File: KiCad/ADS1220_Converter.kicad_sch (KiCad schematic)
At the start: 10 parts, among them U1 ADS1220xPW

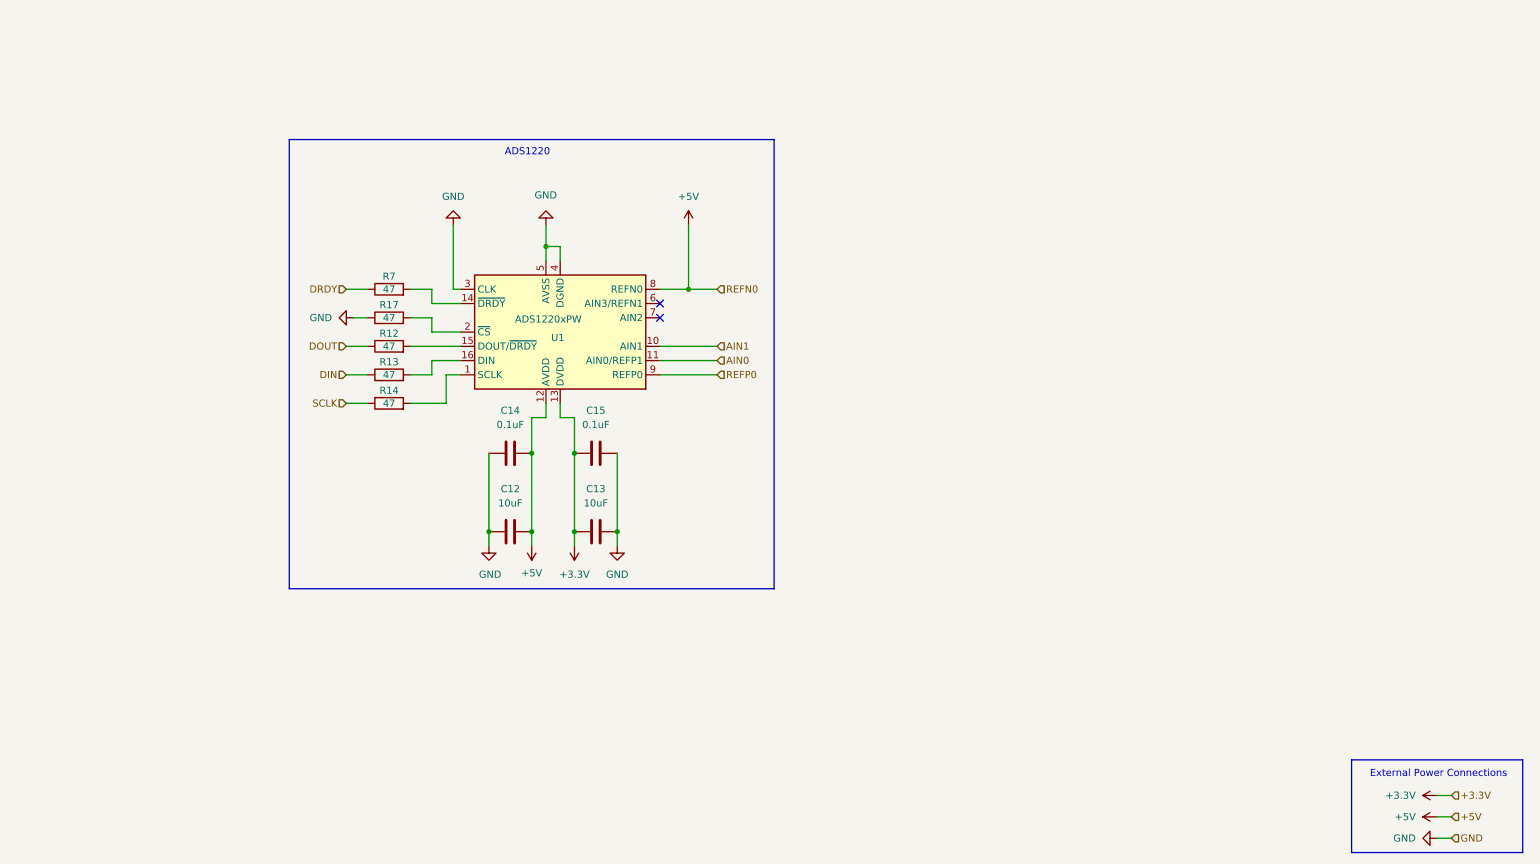
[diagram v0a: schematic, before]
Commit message: Use 12V Power
* Use 12 V Power
* Update to an F103 processor with better compatibility with Katapult
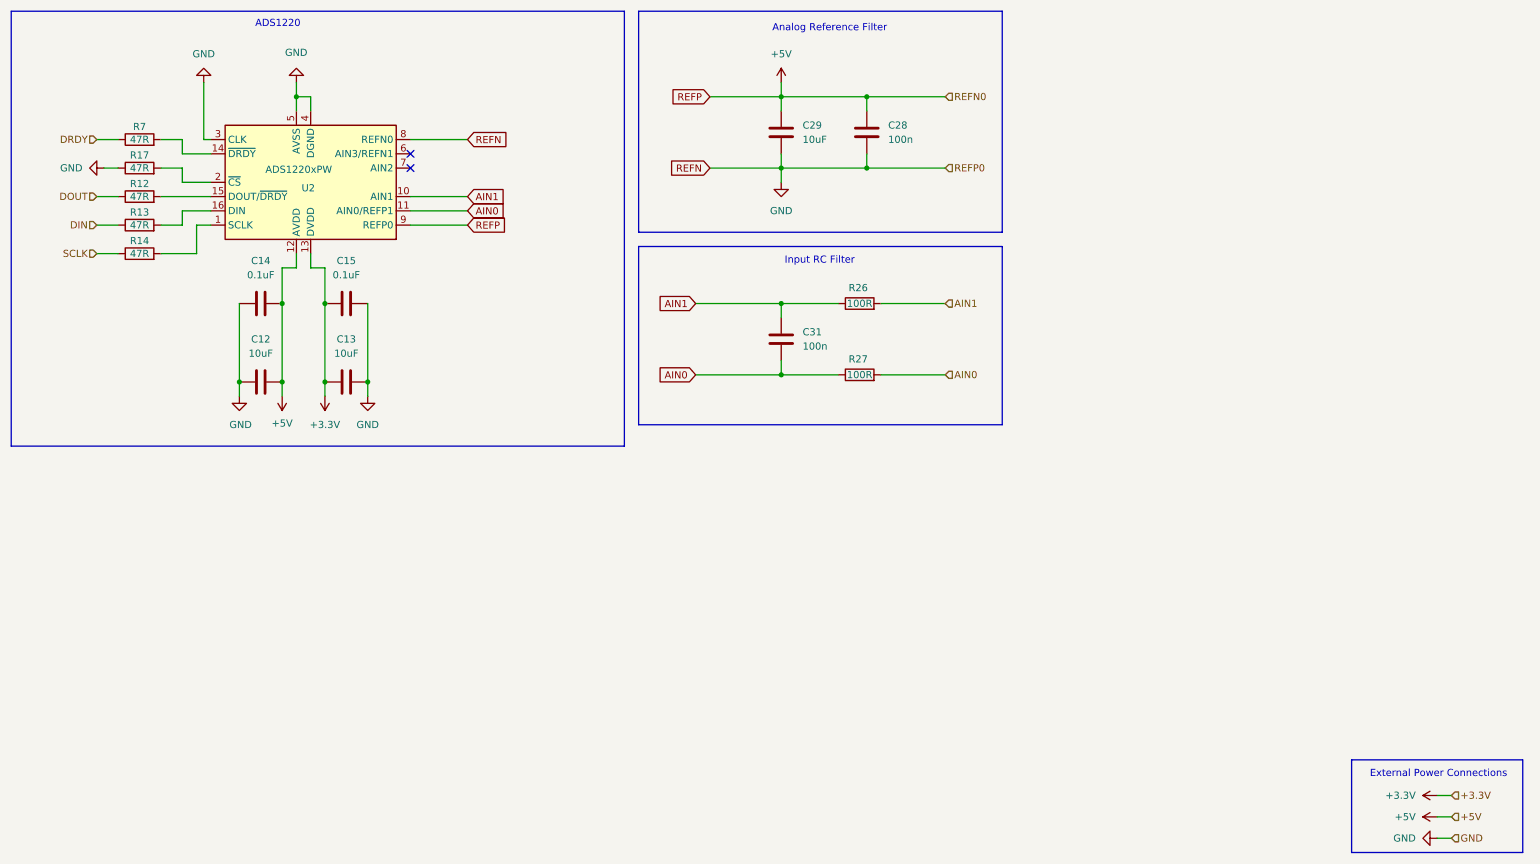
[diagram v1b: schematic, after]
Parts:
- added C28, C31: 100n, Capacitor_SMD:C_0603_1608Metric_Pad1.08x0.95mm_HandSolder, symbol Device:C
- added C29: 10uF, Capacitor_SMD:C_0603_1608Metric_Pad1.08x0.95mm_HandSolder, symbol Device:C
- added R26, R27: 100R, Resistor_SMD:R_0603_1608Metric_Pad0.98x0.95mm_HandSolder, symbol Device:R
- C12, C13, C14, C15: footprint (none) -> Capacitor_SMD:C_0603_1608Metric_Pad1.08x0.95mm_HandSolder
- R12, R13, R14, R17, R7: value 47 -> 47R; footprint (none) -> Resistor_SMD:R_0603_1608Metric_Pad0.98x0.95mm_HandSolder
- renumbered U1 to U2
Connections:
- net REFP0 is gone; now on net +5V: U2.9 (REFP0)
- net +5V: now also C28.1, C29.1; no longer U2.8 (REFN0)
- net AIN0: now also C31.2, R27.1, R27.2
- net AIN1: now also C31.1, R26.1, R26.2
- net GND: now also U2.8 (REFN0), C28.2, C29.2
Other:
- note added: "Analog Reference Filter"
- note added: "Input RC Filter"
- moved on the sheet: C12, C13, C14, C15, R12, R13, R14, R17, R7, U2

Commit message: Update 5V Power Stage
* Update the 5V power stage based on the recommendations from TI.
* Updated standard passive footprint to 0805 hand solder configuration
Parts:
- C12, C13, C14, C15, C28, C29, C31: footprint Capacitor_SMD:C_0603_1608Metric_Pad1.08x0.95mm_HandSolder -> Capacitor_SMD:C_0805_2012Metric_Pad1.18x1.45mm_HandSolder
- R12, R13, R14, R17, R26, R27, R7: footprint Resistor_SMD:R_0603_1608Metric_Pad0.98x0.95mm_HandSolder -> Resistor_SMD:R_0805_2012Metric_Pad1.20x1.40mm_HandSolder
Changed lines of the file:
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@@
 			)
 		)
-		(property "Footprint" "Capacitor_SMD:C_0603_1608Metric_Pad1.08x0.95mm_HandSolder"
+		(property "Footprint" "Capacitor_SMD:C_0805_2012Metric_Pad1.18x1.45mm_HandSolder"
 			(at 152.0952 39.37 0)
 			(effects
@@
 			)
 		)
-		(property "Footprint" "Resistor_SMD:R_0603_1608Metric_Pad0.98x0.95mm_HandSolder"
+		(property "Footprint" "Resistor_SMD:R_0805_2012Metric_Pad1.20x1.40mm_HandSolder"
 			(at 36.83 53.848 90)
 			(effects
@@
 			)
 		)
-		(property "Footprint" "Resistor_SMD:R_0603_1608Metric_Pad0.98x0.95mm_HandSolder"
+		(property "Footprint" "Resistor_SMD:R_0805_2012Metric_Pad1.20x1.40mm_HandSolder"
 			(at 165.1 67.818 90)
 			(effects
@@
 			)
 		)
-		(property "Footprint" "Capacitor_SMD:C_0603_1608Metric_Pad1.08x0.95mm_HandSolder"
+		(property "Footprint" "Capacitor_SMD:C_0805_2012Metric_Pad1.18x1.45mm_HandSolder"
 			(at 167.3352 39.37 0)
 			(effects
@@
 			)
 		)
-		(property "Footprint" "Capacitor_SMD:C_0603_1608Metric_Pad1.08x0.95mm_HandSolder"
+		(property "Footprint" "Capacitor_SMD:C_0805_2012Metric_Pad1.18x1.45mm_HandSolder"
 			(at 152.0952 76.2 0)
 			(effects
@@
 			)
 		)
-		(property "Footprint" "Capacitor_SMD:C_0603_1608Metric_Pad1.08x0.95mm_HandSolder"
+		(property "Footprint" "Capacitor_SMD:C_0805_2012Metric_Pad1.18x1.45mm_HandSolder"
 			(at 77.47 65.0748 0)
 			(effects
@@
 			)
 		)
-		(property "Footprint" "Resistor_SMD:R_0603_1608Metric_Pad0.98x0.95mm_HandSolder"
+		(property "Footprint" "Resistor_SMD:R_0805_2012Metric_Pad1.20x1.40mm_HandSolder"
 			(at 36.83 43.688 90)
 			(effects
@@
 			)
 		)
-		(property "Footprint" "Capacitor_SMD:C_0603_1608Metric_Pad1.08x0.95mm_HandSolder"
+		(property "Footprint" "Capacitor_SMD:C_0805_2012Metric_Pad1.18x1.45mm_HandSolder"
 			(at 62.23 65.0748 0)
 			(effects
@@
 			)
 		)
-		(property "Footprint" "Resistor_SMD:R_0603_1608Metric_Pad0.98x0.95mm_HandSolder"
+		(property "Footprint" "Resistor_SMD:R_0805_2012Metric_Pad1.20x1.40mm_HandSolder"
 			(at 36.83 38.608 90)
 			(effects
@@
 			)
 		)
-		(property "Footprint" "Resistor_SMD:R_0603_1608Metric_Pad0.98x0.95mm_HandSolder"
+		(property "Footprint" "Resistor_SMD:R_0805_2012Metric_Pad1.20x1.40mm_HandSolder"
 			(at 36.83 58.928 90)
 			(effects
@@
 			)
 		)
-		(property "Footprint" "Capacitor_SMD:C_0603_1608Metric_Pad1.08x0.95mm_HandSolder"
+		(property "Footprint" "Capacitor_SMD:C_0805_2012Metric_Pad1.18x1.45mm_HandSolder"
 			(at 77.47 79.0448 0)
 			(effects
@@
 			)
 		)
-		(property "Footprint" "Capacitor_SMD:C_0603_1608Metric_Pad1.08x0.95mm_HandSolder"
+		(property "Footprint" "Capacitor_SMD:C_0805_2012Metric_Pad1.18x1.45mm_HandSolder"
 			(at 62.23 79.0448 0)
 			(effects
@@
 			)
 		)
-		(property "Footprint" "Resistor_SMD:R_0603_1608Metric_Pad0.98x0.95mm_HandSolder"
+		(property "Footprint" "Resistor_SMD:R_0805_2012Metric_Pad1.20x1.40mm_HandSolder"
 			(at 36.83 48.768 90)
 			(effects
@@
 			)
 		)
-		(property "Footprint" "Resistor_SMD:R_0603_1608Metric_Pad0.98x0.95mm_HandSolder"
+		(property "Footprint" "Resistor_SMD:R_0805_2012Metric_Pad1.20x1.40mm_HandSolder"
 			(at 165.1 80.518 90)
 			(effects

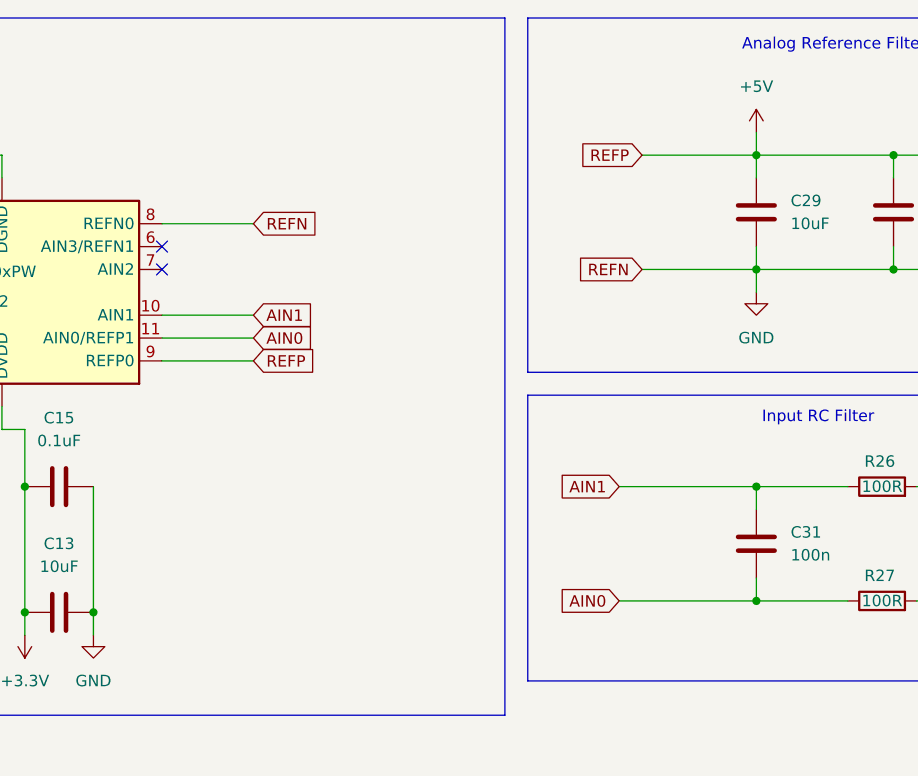
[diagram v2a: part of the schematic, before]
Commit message: Initial Routing
Taking a first pass at layout of the PCB
* load cell connectors were moved to the root schematic and placed on a bus to facilitate PCB routing
* Nets for the filters were directly connected to remove the confusion about GND verses REFN
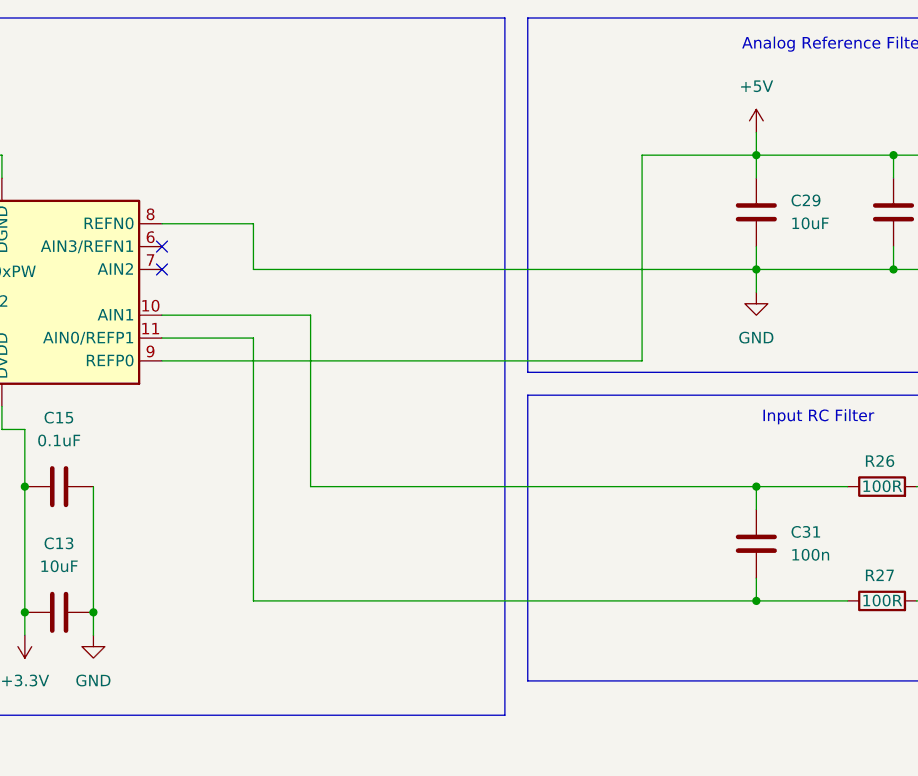
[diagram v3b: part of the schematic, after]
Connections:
- net AIN0: no longer C31.2, R27.1, U2.11 (AIN0/REFP1)
- net AIN1: no longer C31.1, R26.1, U2.10 (AIN1)
- new net: C31.1, R26.1, U2.10 (AIN1)
- new net: C31.2, R27.1, U2.11 (AIN0/REFP1)
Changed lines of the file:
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@@
 	(wire
 		(pts
-			(xy 95.25 46.99) (xy 85.09 46.99)
+			(xy 85.09 46.99) (xy 101.6 46.99)
 		)
 		(stroke
@@
 	(wire
 		(pts
-			(xy 85.09 52.07) (xy 95.25 52.07)
+			(xy 85.09 52.07) (xy 138.43 52.07)
+		)
+		(stroke
+			(width 0)
+			(type default)
+		)
+	)
+	(wire
+		(pts
+			(xy 95.25 41.91) (xy 95.25 36.83)
 		)
 		(stroke
@@
 	(wire
 		(pts
-			(xy 138.43 41.91) (xy 151.13 41.91)
-		)
-		(stroke
-			(width 0)
-			(type default)
-		)
-	)
-	(wire
-		(pts
 			(xy 168.91 66.04) (xy 180.34 66.04)
 		)
@@
 	(wire
 		(pts
+			(xy 101.6 66.04) (xy 151.13 66.04)
+		)
+		(stroke
+			(width 0)
+			(type default)
+		)
+	)
+	(wire
+		(pts
 			(xy 69.85 59.69) (xy 69.85 66.04)
 		)
@@
 	(wire
 		(pts
+			(xy 95.25 41.91) (xy 151.13 41.91)
+		)
+		(stroke
+			(width 0)
+			(type default)
+		)
+	)
+	(wire
+		(pts
 			(xy 151.13 41.91) (xy 166.37 41.91)
 		)
@@
 	(wire
 		(pts
-			(xy 135.89 78.74) (xy 151.13 78.74)
-		)
-		(stroke
-			(width 0)
-			(type default)
-		)
-	)
-	(wire
-		(pts
 			(xy 29.21 52.07) (xy 33.02 52.07)
 		)
@@
 	(wire
 		(pts
-			(xy 135.89 66.04) (xy 151.13 66.04)
-		)
-		(stroke
-			(width 0)
-			(type default)
-		)
-	)
-	(wire
-		(pts
 			(xy 62.23 59.69) (xy 64.77 59.69)
 		)
@@
 	(wire
 		(pts
+			(xy 138.43 52.07) (xy 138.43 29.21)
+		)
+		(stroke
+			(width 0)
+			(type default)
+		)
+	)
+	(wire
+		(pts
 			(xy 44.45 41.91) (xy 44.45 44.45)
 		)
@@
 	(wire
 		(pts
+			(xy 95.25 49.53) (xy 95.25 78.74)
+		)
+		(stroke
+			(width 0)
+			(type default)
+		)
+	)
+	(wire
+		(pts
 			(xy 67.31 59.69) (xy 67.31 57.15)
 		)
@@
 	(wire
 		(pts
+			(xy 95.25 78.74) (xy 151.13 78.74)
+		)
+		(stroke
+			(width 0)
+			(type default)
+		)
+	)
+	(wire
+		(pts
 			(xy 62.23 59.69) (xy 62.23 66.04)
 		)
@@
 		(pts
 			(xy 69.85 66.04) (xy 69.85 80.01)
+		)
+		(stroke
+			(width 0)
+			(type default)
+		)
+	)
+	(wire
+		(pts
+			(xy 101.6 46.99) (xy 101.6 66.04)
 		)
 		(stroke
@@
 			)
 		)
-	)
-	(global_label "AIN0"
-		(shape input)
-		(at 95.25 49.53 0)
-		(fields_autoplaced yes)
-		(effects
-			(font
-				(size 1.27 1.27)
-			)
-			(justify left)
-		)
-		(property "Intersheetrefs" "${INTERSHEET_REFS}"
-			(at 102.4686 49.53 0)
-			(effects
-				(font
-					(size 1.27 1.27)
-				)
-				(justify left)
-				(hide yes)
-			)
-		)
-	)
-	(global_label "REFP"
-		(shape input)
-		(at 95.25 52.07 0)
-		(fields_autoplaced yes)
-		(effects
-			(font
-				(size 1.27 1.27)
-			)
-			(justify left)
-		)
-		(property "Intersheetrefs" "${INTERSHEET_REFS}"
-			(at 103.0128 52.07 0)
-			(effects
-				(font
-					(size 1.27 1.27)
-				)
-				(justify left)
-				(hide yes)
-			)
-		)
-	)
-	(global_label "REFN"
-		(shape input)
-		(at 138.43 41.91 180)
-		(fields_autoplaced yes)
-		(effects
-			(font
-				(size 1.27 1.27)
-			)
-			(justify right)
-		)
-		(property "Intersheetrefs" "${INTERSHEET_REFS}"
-			(at 130.6067 41.91 0)
-			(effects
-				(font
-					(size 1.27 1.27)
-				)
-				(justify right)
-				(hide yes)
-			)
-		)
-	)
-	(global_label "AIN1"
-		(shape input)
-		(at 95.25 46.99 0)
-		(fields_autoplaced yes)
-		(effects
-			(font
-				(size 1.27 1.27)
-			)
-			(justify left)
-		)
-		(property "Intersheetrefs" "${INTERSHEET_REFS}"
-			(at 102.4686 46.99 0)
-			(effects
-				(font
-					(size 1.27 1.27)
-				)
-				(justify left)
-				(hide yes)
-			)
-		)
-	)
-	(global_label "REFN"
-		(shape input)
-		(at 95.25 36.83 0)
-		(fields_autoplaced yes)
-		(effects
-			(font
-				(size 1.27 1.27)
-			)
-			(justify left)
-		)
-		(property "Intersheetrefs" "${INTERSHEET_REFS}"
-			(at 103.0733 36.83 0)
-			(effects
-				(font
-					(size 1.27 1.27)
-				)
-				(justify left)
-				(hide yes)
-			)
-		)
-	)
-	(global_label "AIN0"
-		(shape input)
-		(at 135.89 78.74 180)
-		(fields_autoplaced yes)
-		(effects
-			(font
-				(size 1.27 1.27)
-			)
-			(justify right)
-		)
-		(property "Intersheetrefs" "${INTERSHEET_REFS}"
-			(at 128.6714 78.74 0)
-			(effects
-				(font
-					(size 1.27 1.27)
-				)
-				(justify right)
-				(hide yes)
-			)
-		)
-	)
-	(global_label "REFP"
-		(shape input)
-		(at 138.43 29.21 180)
-		(fields_autoplaced yes)
-		(effects
-			(font
-				(size 1.27 1.27)
-			)
-			(justify right)
-		)
-		(property "Intersheetrefs" "${INTERSHEET_REFS}"
-			(at 130.6672 29.21 0)
-			(effects
-				(font
-					(size 1.27 1.27)
-				)
-				(justify right)
-				(hide yes)
-			)
-		)
-	)
-	(global_label "AIN1"
-		(shape input)
-		(at 135.89 66.04 180)
-		(fields_autoplaced yes)
-		(effects
-			(font
-				(size 1.27 1.27)
-			)
-			(justify right)
-		)
-		(property "Intersheetrefs" "${INTERSHEET_REFS}"
-			(at 128.6714 66.04 0)
-			(effects
-				(font
-					(size 1.27 1.27)
-				)
-				(justify right)
-				(hide yes)
-			)
-		)
